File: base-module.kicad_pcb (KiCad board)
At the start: 4 copper layers, 114 parts, among them J200 09031967921, J401 USB_C_Receptacle_USB2.0_16P, Q700 S9013, U300 TPS563201DDCR, U301 TPS563201DDCR, U401 W25Q128, U402 TS3USB30ERSWR, U403 IP4234CZ6,115, U404 IP4234CZ6,115, U405 TJA1044GTK_3Z, U406 CH334R, U407 STM32F750V8Tx, U408 TJA1044GTK_3Z, U700 STM32F103CBTx, X402 X322512MSB4SI, X700 X50328MSB2GI, Y403 12Mhz

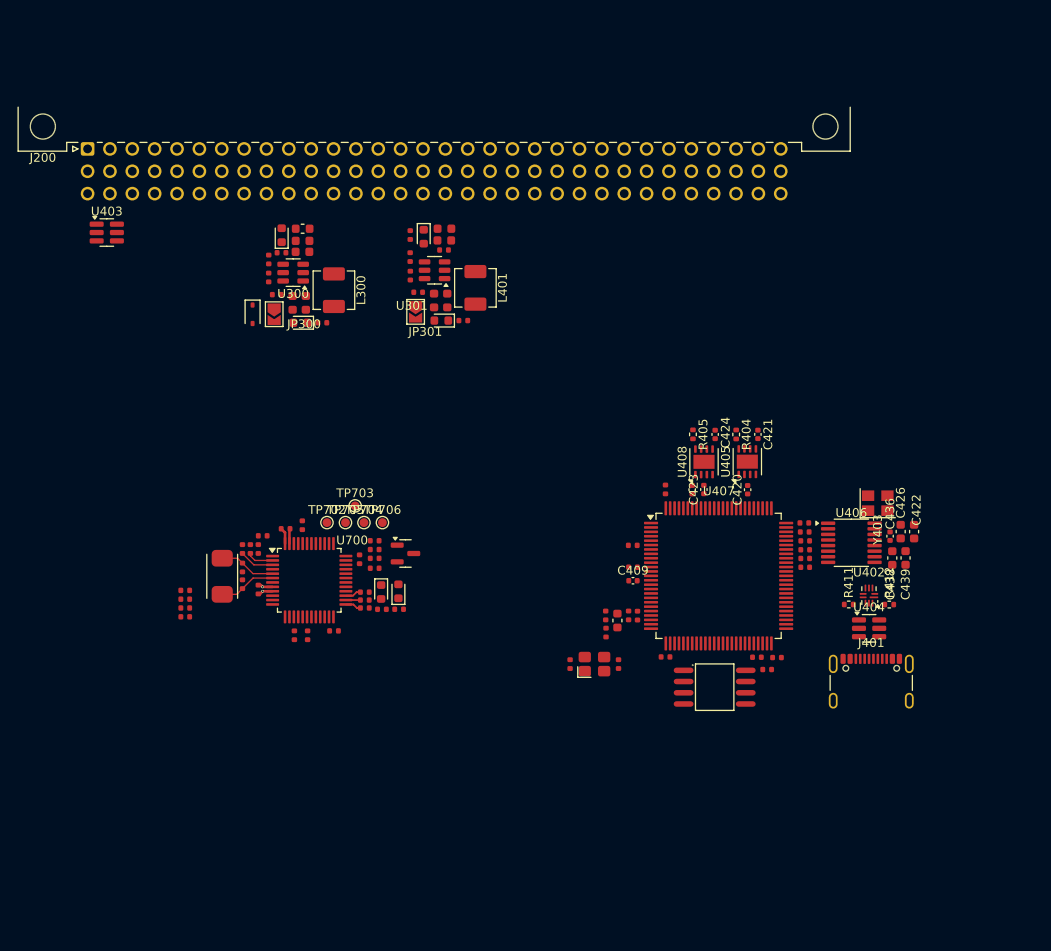
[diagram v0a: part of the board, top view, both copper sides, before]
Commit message: [2] Change USB connector, add board outline and information about keepout area
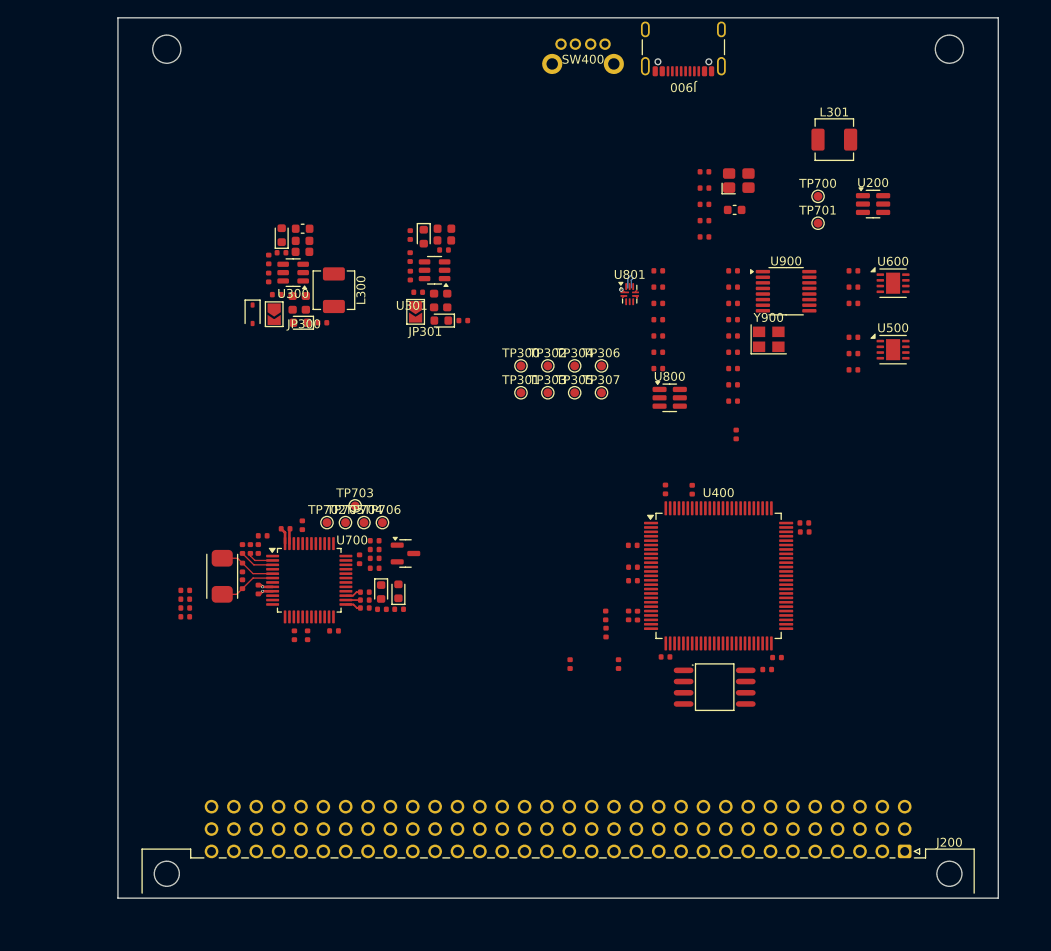
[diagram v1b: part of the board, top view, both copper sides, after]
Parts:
- removed C419: 2.2uF, PCM_JLCPCB:C_0402
- removed C420, C421, C423, C424: 100nF, Capacitor_SMD:C_0402_1005Metric
- removed C422, C438: 10u, Capacitor_SMD:C_0603_1608Metric
- removed C426: 1u, Capacitor_SMD:C_0603_1608Metric
- removed C436: 100n, Capacitor_SMD:C_0402_1005Metric
- removed C439: 100n, Capacitor_SMD:C_0603_1608Metric
- removed FB401: ~, PCM_JLCPCB:FB_0603
- removed J401: USB_C_Receptacle_USB2.0_16P, Connector_USB:USB_C_Receptacle_GCT_USB4105-xx-A_16P_TopMnt_Horizontal
- removed L401: 3.3uH, Inductor_SMD:L_Changjiang_FXL0420
- removed R405, R411, R412: 10k, Resistor_SMD:R_0402_1005Metric
- removed R443, R444, R445, R446: 22Ω, PCM_JLCPCB:R_0402
- removed U402: TS3USB30ERSWR, Package_DFN_QFN:UQFN-10_1.4x1.8mm_P0.4mm
- removed U403, U404: IP4234CZ6,115, Package_TO_SOT_SMD:SC-74-6_1.55x2.9mm_P0.95mm
- removed U405, U408: TJA1044GTK_3Z, Package_SON:HVSON-8-1EP_3x3mm_P0.65mm_EP1.6x2.4mm
- removed U406: CH334R, Package_SO:QSOP-16_3.9x4.9mm_P0.635mm
- removed U407: STM32F750V8Tx, Package_QFP:LQFP-100_14x14mm_P0.5mm
- removed X402: X322512MSB4SI, PCM_JLCPCB:CRYSTAL-SMD_4P-L3.2-W2.5-BL
- removed Y403: 12Mhz, Crystal:Crystal_SMD_3225-4Pin_3.2x2.5mm
- added C400: 10uF, PCM_JLCPCB:C_0402, F.Cu at (105.9, 86.6)
- added C500: 100nF, PCM_JLCPCB:C_0402, F.Cu at (122.8, 105.4)
- added C501: 100nF, PCM_JLCPCB:C_0402, F.Cu at (122.8, 107.2)
- added C600: 100nF, PCM_JLCPCB:C_0402, F.Cu at (122.8, 97.8)
- added C601: 100nF, PCM_JLCPCB:C_0402, F.Cu at (122.8, 99.7)
- added C800: 100nF, PCM_JLCPCB:C_0402, F.Cu at (100.6, 97.8)
- added C801: 100nF, PCM_JLCPCB:C_0402, F.Cu at (100.6, 99.7)
- added C900: 100nF, PCM_JLCPCB:C_0402, F.Cu at (109.1, 97.8)
- added C901: 1uF, PCM_JLCPCB:C_0402, F.Cu at (109.1, 99.7)
- added C902: 10uF, PCM_JLCPCB:C_0402, F.Cu at (109.1, 101.5)
- added C903: 100nF, PCM_JLCPCB:C_0402, F.Cu at (109.1, 103.4)
- added C904: 1uF, PCM_JLCPCB:C_0402, F.Cu at (109.1, 105.2)
- added FB400: ~, PCM_JLCPCB:FB_0603, F.Cu at (109.3, 90.9)
- added J900: USB_C_Receptacle_USB2.0_16P, Connector_USB:USB_C_Receptacle_GCT_USB4105-xx-A_16P_TopMnt_Horizontal, F.Cu at (103.5, 71.5)
- added L301: 3.3uH, Inductor_SMD:L_Changjiang_FXL0420, F.Cu at (120.6, 82.9)
- added R400: 1kΩ, PCM_JLCPCB:R_0402, F.Cu at (105.9, 88.5)
- added R401: 1kΩ, PCM_JLCPCB:R_0402, F.Cu at (105.9, 90.3)
- added R402: 10kΩ, PCM_JLCPCB:R_0402, F.Cu at (105.9, 92.2)
- added R403: 10kΩ, PCM_JLCPCB:R_0402, F.Cu at (105.9, 94.0)
- added R500: 10kΩ, PCM_JLCPCB:R_0402, F.Cu at (122.8, 109.1)
- added R600: 10kΩ, PCM_JLCPCB:R_0402, F.Cu at (122.8, 101.5)
- added R800: 10kΩ, PCM_JLCPCB:R_0402, F.Cu at (100.6, 101.5)
- added R801: 10kΩ, PCM_JLCPCB:R_0402, F.Cu at (100.6, 103.4)
- added R802: 330Ω, PCM_JLCPCB:R_0402, F.Cu at (100.6, 105.2)
- added R900: 22Ω, PCM_JLCPCB:R_0402, F.Cu at (109.1, 107.1)
- added R901: 22Ω, PCM_JLCPCB:R_0402, F.Cu at (109.1, 109.0)
- added R902: 22Ω, PCM_JLCPCB:R_0402, F.Cu at (109.1, 110.8)
- added R903: 22Ω, PCM_JLCPCB:R_0402, F.Cu at (109.1, 112.7)
- added R904: 5.1kΩ, PCM_JLCPCB:R_0402, F.Cu at (100.6, 107.1)
- added R905: 5.1kΩ, PCM_JLCPCB:R_0402, F.Cu at (100.6, 109.0)
- added SW400: TL2243, kicad-footprints:TL2243, F.Cu at (92.1, 74.3)
- added TP300: TestPoint, TestPoint:TestPoint_Pad_D1.0mm, F.Cu at (85.0, 108.7)
- added TP301: TestPoint, TestPoint:TestPoint_Pad_D1.0mm, F.Cu at (85.0, 111.7)
- added TP302: TestPoint, TestPoint:TestPoint_Pad_D1.0mm, F.Cu at (88.1, 108.7)
- added TP303: Buck Feedback, TestPoint:TestPoint_Pad_D1.0mm, F.Cu at (88.1, 111.7)
- added TP304: TestPoint, TestPoint:TestPoint_Pad_D1.0mm, F.Cu at (91.2, 108.7)
- added TP305: TestPoint, TestPoint:TestPoint_Pad_D1.0mm, F.Cu at (91.2, 111.7)
- added TP306: TestPoint, TestPoint:TestPoint_Pad_D1.0mm, F.Cu at (94.2, 108.7)
- added TP307: Buck Feedback, TestPoint:TestPoint_Pad_D1.0mm, F.Cu at (94.2, 111.7)
- added TP700: TestPoint, TestPoint:TestPoint_Pad_D1.0mm, F.Cu at (118.8, 89.4)
- added TP701: TestPoint, TestPoint:TestPoint_Pad_D1.0mm, F.Cu at (118.8, 92.4)
- added U200: IP4234CZ6,115, Package_TO_SOT_SMD:SC-74-6_1.55x2.9mm_P0.95mm, F.Cu at (125.0, 90.3)
- added U400: STM32F750V8Tx, Package_QFP:LQFP-100_14x14mm_P0.5mm, F.Cu at (107.5, 132.5)
- added U500: TJA1044GTK_3Z, Package_SON:HVSON-8-1EP_3x3mm_P0.65mm_EP1.6x2.4mm, F.Cu at (127.3, 106.8)
- added U600: TJA1044GTK_3Z, Package_SON:HVSON-8-1EP_3x3mm_P0.65mm_EP1.6x2.4mm, F.Cu at (127.3, 99.3)
- added U800: IP4234CZ6,115, Package_TO_SOT_SMD:SC-74-6_1.55x2.9mm_P0.95mm, F.Cu at (101.9, 112.3)
- added U801: TS3USB30ERSWR, Package_DFN_QFN:UQFN-10_1.4x1.8mm_P0.4mm, F.Cu at (97.4, 100.5)
- added U900: CH334R, Package_SO:QSOP-16_3.9x4.9mm_P0.635mm, F.Cu at (115.2, 100.2)
- added X400: X322512MSB4SI, PCM_JLCPCB:CRYSTAL-SMD_4P-L3.2-W2.5-BL, F.Cu at (109.8, 87.6)
- added Y900: 12Mhz, Crystal:Crystal_SMD_3225-4Pin_3.2x2.5mm, F.Cu at (113.2, 105.6)
- C405, C407: value 10uF -> 100nF
- C406: value 100nF -> 10uF
- C408: value 22pF -> 10uF
- C409: footprint Capacitor_SMD:C_0402_1005Metric -> PCM_JLCPCB:C_0402
- C410: value 100nF -> 4.7uF
- C411: value 10uF -> 22pF
- C412: value 4u7 -> 22pF; footprint Capacitor_SMD:C_0402_1005Metric -> PCM_JLCPCB:C_0402
- C413: value 22pF -> 2.2uF
- C414: value 100nF -> 2.2uF
- C415: value 2.2uF -> 100nF
- R404: value 10k -> 100Ω; footprint Resistor_SMD:R_0402_1005Metric -> PCM_JLCPCB:R_0402
- moved J200 122.4 mm to (128.6, 163.8), turned to 180 degrees
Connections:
- net /ST-LINK/SWD.SWCLK renamed /MCU/SWD.SWCLK
- net /ST-LINK/USB.D+ renamed /ST-LINK/ST-LINK.D+
- C406 pad 1: +3V3 -> Net-(U400-VDDA)
- C407 pad 1: Net-(U407-VDDA) -> Net-(U400-VDDA)
- C408 pad 1: /MCU/OSC_IN -> +3V3
- C409 pad 1: GND -> +3V3
- C409 pad 2: /MCU/NRST -> GND
- C410 pad 1: Net-(U407-VDDA) -> /MCU/BOOT0
- C411 pad 1: +3V3 -> /MCU/OSC_OUT
- C412 pad 1: GND -> /MCU/OSC_IN
- C412 pad 2: /MCU/BOOT0 -> GND
- C413 pad 1: /MCU/OSC_OUT -> /MCU/VCAP_1
- C414 pad 1: +3V3 -> /MCU/VCAP_2
- C415 pad 1: /MCU/VCAP_2 -> /MCU/NRST
- J200 pad a2: /Backplane/USB1U.D- -> /Backplane/BACKPLANE_U.D+
- J200 pad b5: /Backplane/CAN1..+ -> /Backplane/CAN1.+
- J200 pad b6: /Backplane/CAN1..- -> /Backplane/CAN1.-
- J200 pad b8: /Backplane/CAN2..+ -> /Backplane/CAN2.+
- J200 pad b9: /Backplane/CAN2..- -> /Backplane/CAN2.-
- J200 pad c2: /Backplane/USB1U.D+ -> /Backplane/BACKPLANE_U.D-
- J200 pad c5: /Backplane/CAN1..+ -> /Backplane/CAN1.+
- J200 pad c6: /Backplane/CAN1..- -> /Backplane/CAN1.-
- J200 pad c8: /Backplane/CAN2..+ -> /Backplane/CAN2.+
- J200 pad c9: /Backplane/CAN2..- -> /Backplane/CAN2.-
- R404 pad 1: GND -> /MCU/NRST
- R404 pad 2: Net-(U405-STB) -> /MCU/SWD.~{RST}
- R708 pad 1: /ST-LINK/~{RST} -> /MCU/SWD.~{RST}
- R716 pad 1: /ST-LINK/SWD.SWDIO -> /MCU/SWD.SWDIO
- U401 pad 1: /MCU/QSPI1.SCLK -> /MCU/QSPI1.CS
- U700 pad 32: /ST-LINK/USB.D- -> /ST-LINK/ST-LINK.D-
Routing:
- net /USB/USB2S.D+: track 0.00 -> 2.25 mm, vias 0 -> 1
- net /USB/USB2S.D-: track 0.00 -> 1.61 mm
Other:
- board outline added: 100 x 100 mm
- board text added: "DON'T PUT ANYTHING HERE"
